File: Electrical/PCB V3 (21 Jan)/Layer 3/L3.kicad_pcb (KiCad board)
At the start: 2 copper layers, 129.9 x 110 mm, 28 parts, among them J1 Conn_01x06, J2 Conn_02x04_Odd_Even, J3 Conn_01x06, J4 Conn_01x06, J5 Conn_01x06, U2 113991054, U3 4754

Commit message: .
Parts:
- moved J2 15.5 mm to (253.7, 84.5)
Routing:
- net /TX (L3 ESP32): track 77.0 -> 94.8 mm
- net /RX (L3 ESP32): track 94.6 -> 112.0 mm
- net /RX (CAM): track 84.5 -> 68.2 mm
- net +3V3: track 357.9 -> 344.6 mm, vias 8 -> 9
- net /TX (CAM): track 82.5 -> 70.4 mm
- net /RX (IMU): track 43.3 -> 41.1 mm
- net /TX (IMU): track 39.7 -> 38.6 mm

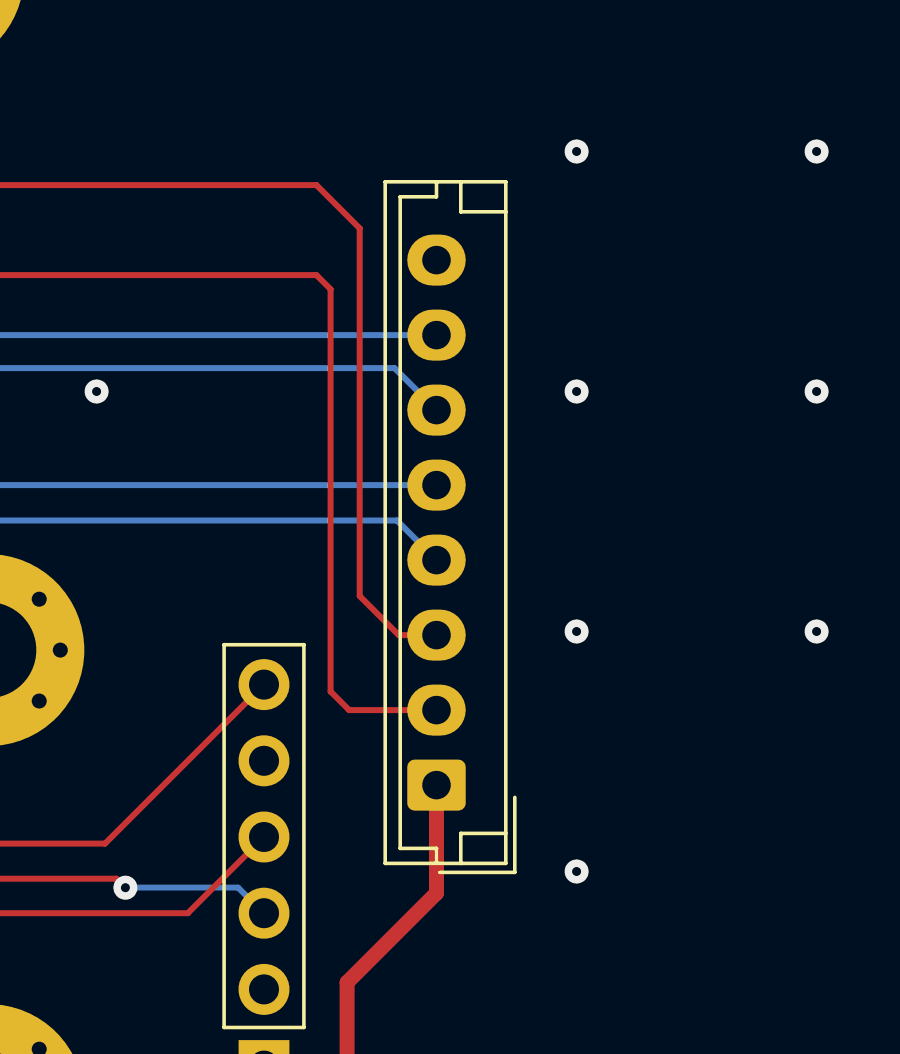
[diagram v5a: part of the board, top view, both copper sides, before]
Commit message: flipped l3 jst, added l3 step
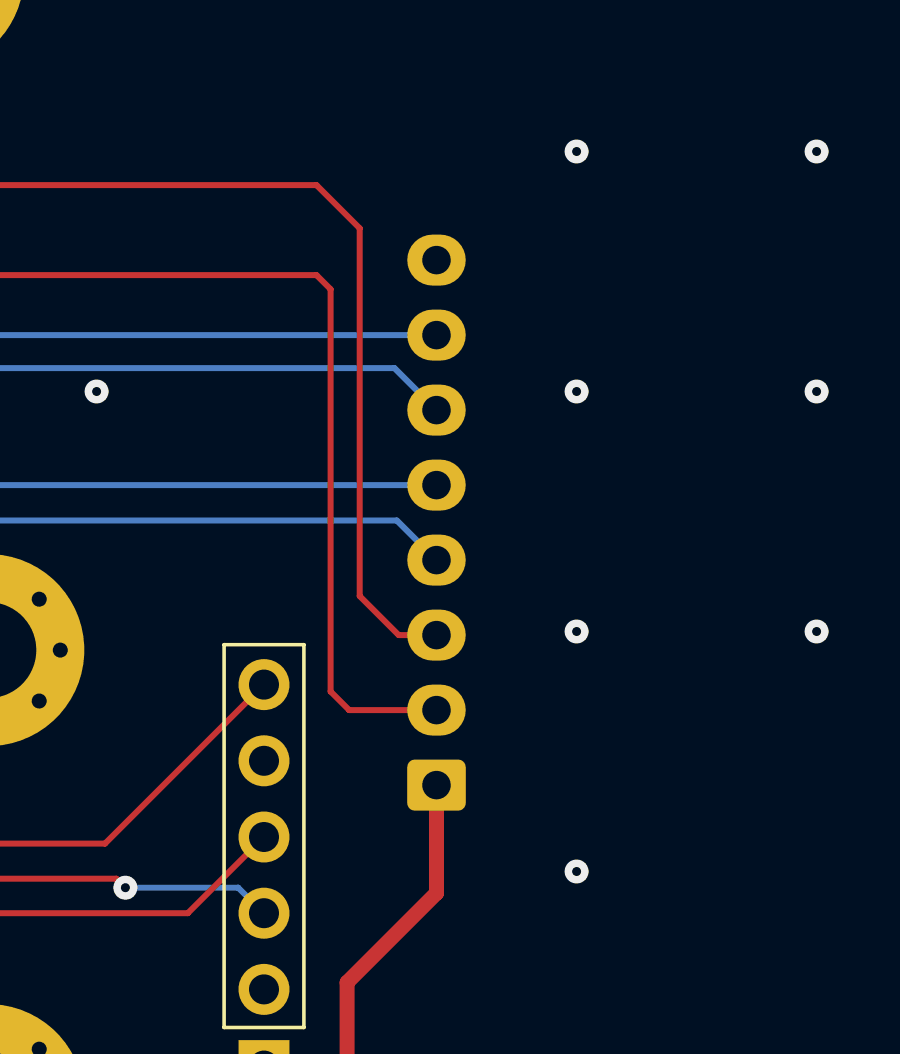
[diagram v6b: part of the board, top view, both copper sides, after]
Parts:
- J2: moved to B.Cu

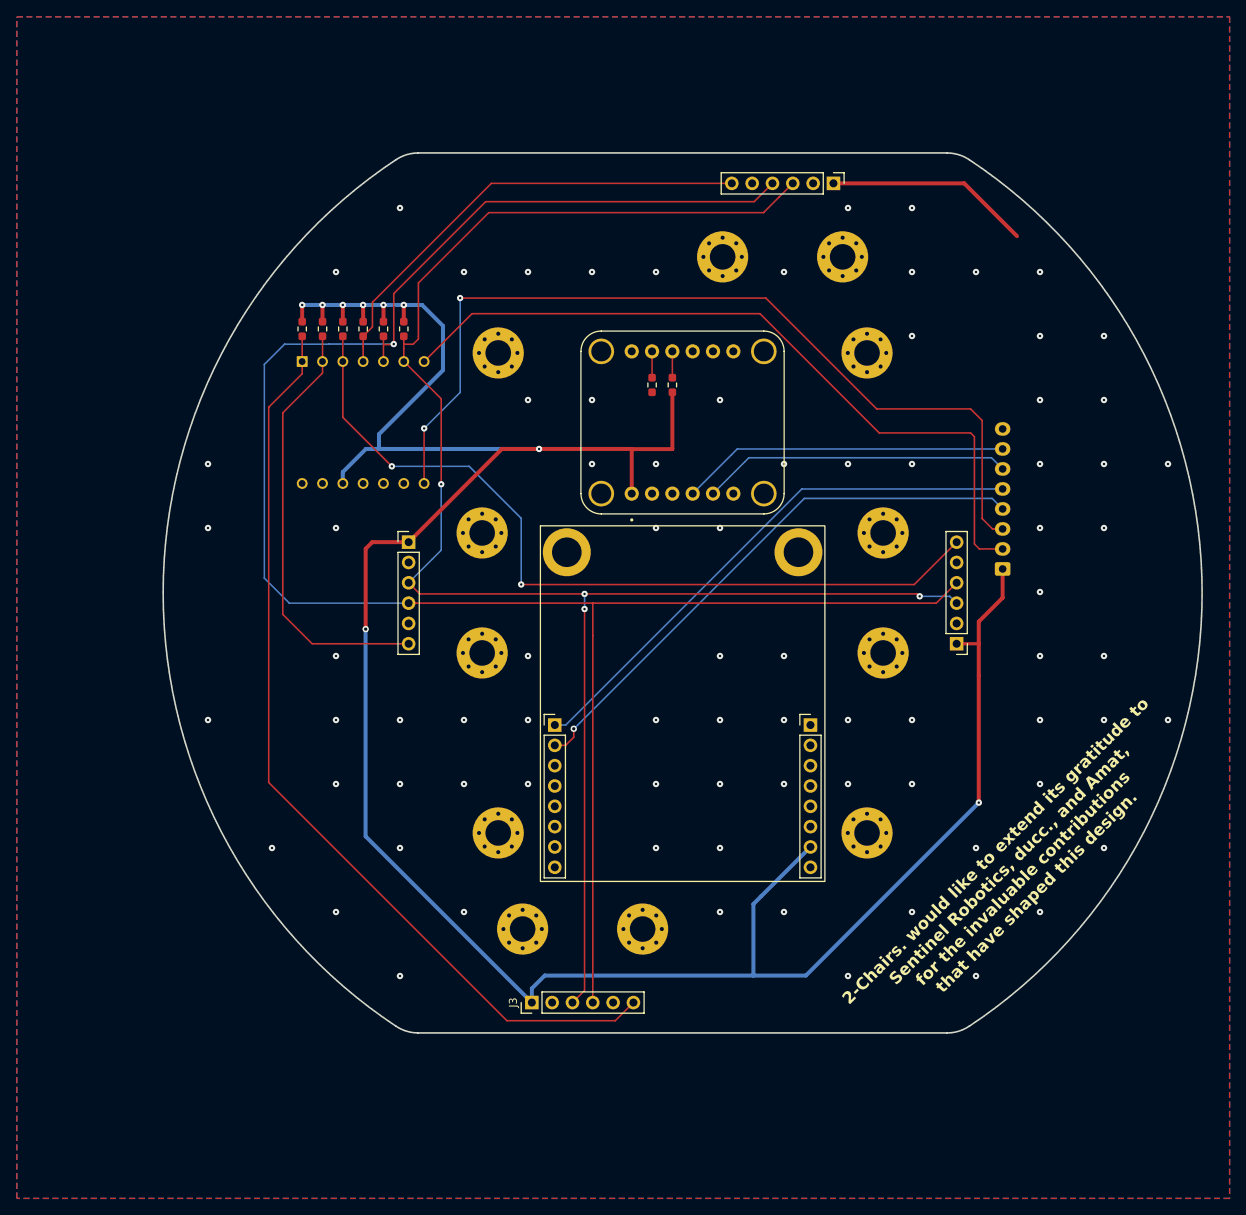
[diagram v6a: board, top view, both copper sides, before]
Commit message: added l3 new step, added new testpoint, fixed some l3
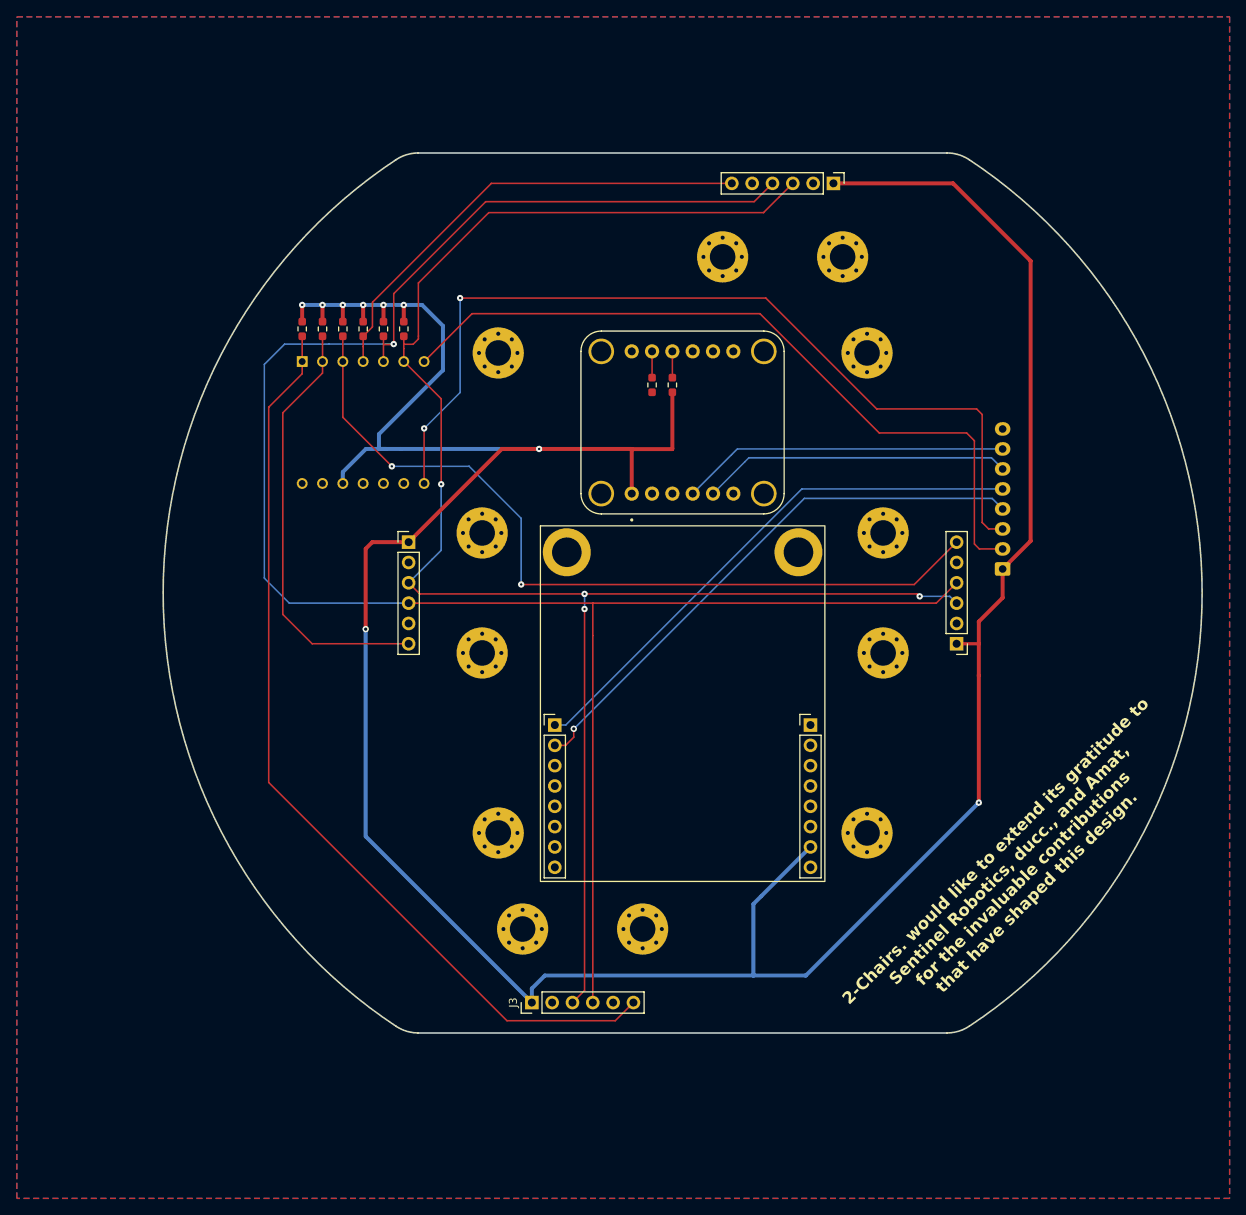
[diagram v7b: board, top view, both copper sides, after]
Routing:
- net +3V3: track 344.6 -> 387.6 mm
- net /RX (L3 ESP32): track 112.0 -> 112.7 mm
- net GND: vias 80 -> 0

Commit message: fixed l3, added new l3 model
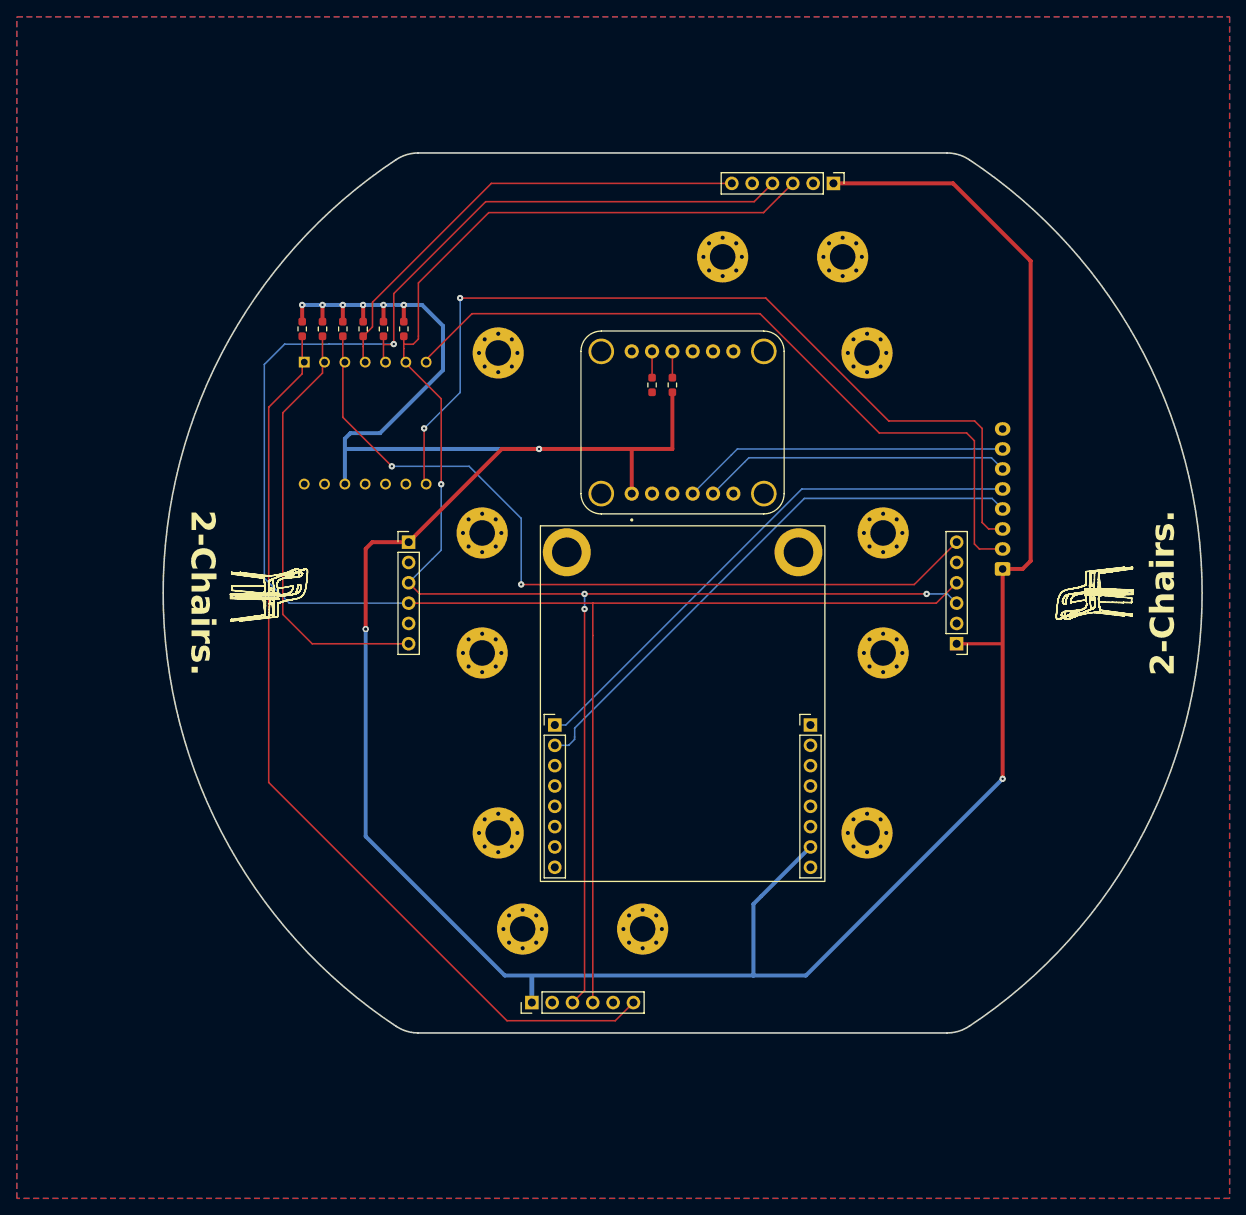
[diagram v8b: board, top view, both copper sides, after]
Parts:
- moved U2 0.27 mm to (174.0, 66.3)
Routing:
- net +3V3: track 387.6 -> 396.0 mm
- net /RX (L3 ESP32): track 112.7 -> 111.7 mm
- net /TX (CAM): track 70.4 -> 70.6 mm, vias 1 -> 0
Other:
- board text removed: "2-Chairs. would like to extend its gratitude to Sentinel Robotics, ducc., and Amat, for the invaluable contributions that have shaped this design."
